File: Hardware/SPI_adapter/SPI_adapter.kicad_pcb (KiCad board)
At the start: 4 copper layers, 99.5 x 34.5 mm, 5 parts, among them J1 Conn_02x07_Top_Bottom, J2 Conn_Coaxial, U1 RF-LORA-868-SO

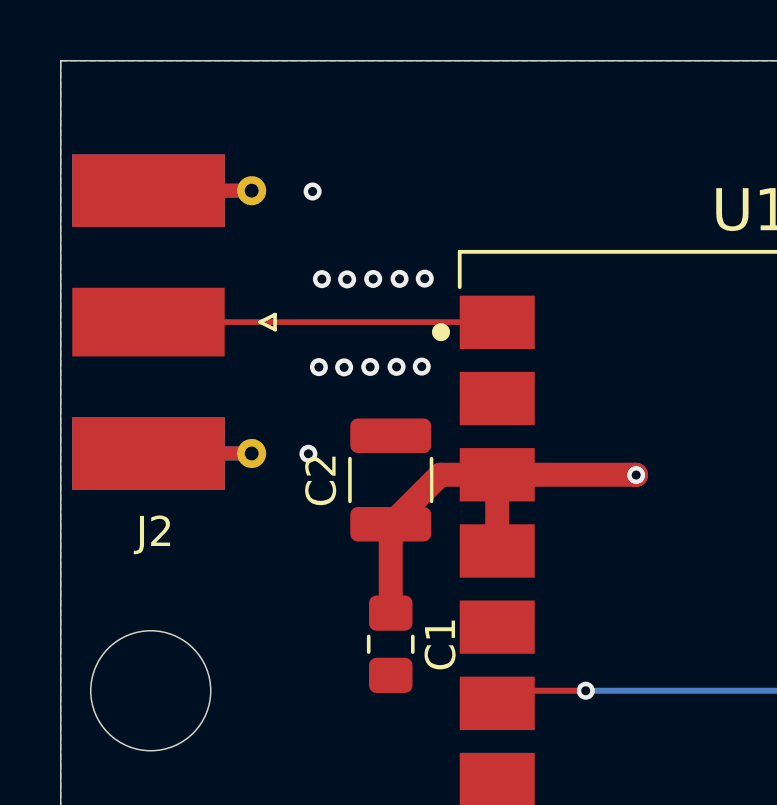
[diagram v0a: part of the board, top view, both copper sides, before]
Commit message: Fixed RF trace, Added new Diodes, better power traces and new switches
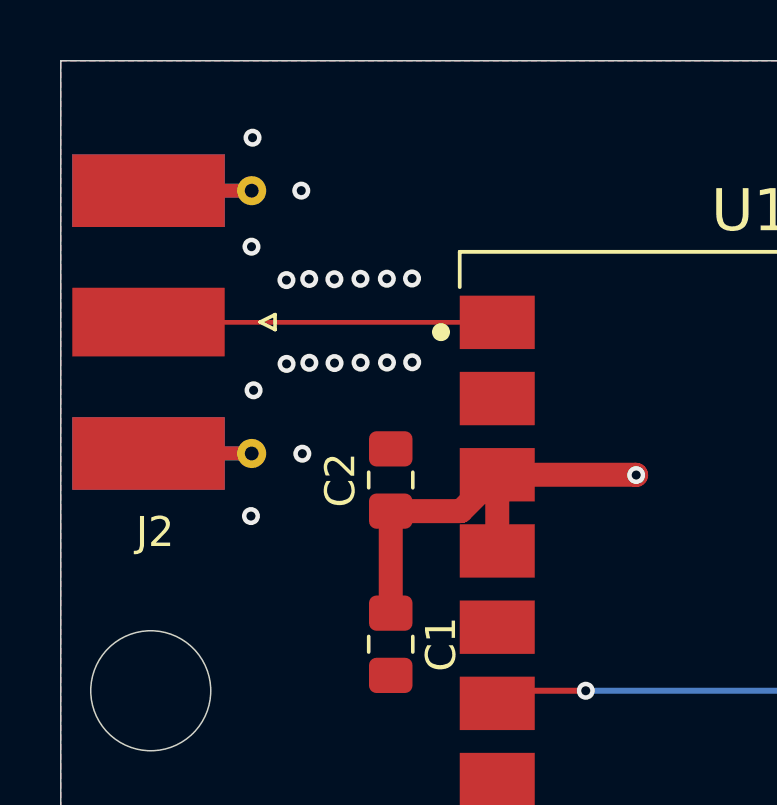
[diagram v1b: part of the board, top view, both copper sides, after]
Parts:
- C2: footprint Capacitor_SMD:C_1210_3225Metric -> Capacitor_SMD:C_0805_2012Metric_Pad1.18x1.45mm_HandSolder
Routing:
- net GND: vias 22 -> 28
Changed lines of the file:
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@@
 		)
 	)
-	(footprint "Capacitor_SMD:C_1210_3225Metric"
+	(footprint "Capacitor_SMD:C_0805_2012Metric_Pad1.18x1.45mm_HandSolder"
 		(layer "F.Cu")
 		(at 88.5 106.475 90)
-		(descr "Capacitor SMD 1210 (3225 Metric), square (rectangular) end terminal, IPC-7351 nominal, (Body size source: IPC-SM-782 page 76, https://www.pcb-3d.com/wordpress/wp-content/uploads/ipc-sm-782a_amendment_1_and_2.pdf), generated with kicad-footprint-generator")
-		(tags "capacitor")
+		(descr "Capacitor SMD 0805 (2012 Metric), square (rectangular) end terminal, IPC-7351 nominal with elongated pad for handsoldering. (Body size source: IPC-SM-782 page 76, https://www.pcb-3d.com/wordpress/wp-content/uploads/ipc-sm-782a_amendment_1_and_2.pdf, https://docs.google.com/spreadsheets/d/1BsfQQcO9C6DZCsRaXUlFlo91Tg2WpOkGARC1WS5S8t0/edit?usp=sharing), generated with kicad-footprint-generator")
+		(tags "capacitor handsolder")
 		(property "Reference" "C2"
-			(at 0 -2.3 90)
+			(at 0 -1.68 90)
 			(layer "F.SilkS")
 			(effects
@@
 		)
 		(property "Value" "4.7µF"
-			(at 0 2.3 90)
-			(layer "F.Fab")
-			(hide yes)
+			(at 0 1.68 90)
+			(layer "F.Fab")
 			(effects
 				(font
@@
 		(attr smd)
 		(fp_line
-			(start -0.711252 -1.36)
-			(end 0.711252 -1.36)
+			(start -0.261252 -0.735)
+			(end 0.261252 -0.735)
 			(stroke
 				(width 0.12)
@@
 		)
 		(fp_line
-			(start -0.711252 1.36)
-			(end 0.711252 1.36)
+			(start -0.261252 0.735)
+			(end 0.261252 0.735)
 			(stroke
 				(width 0.12)
@@
 		)
 		(fp_rect
-			(start -2.3 -1.6)
-			(end 2.3 1.6)
+			(start -1.88 -0.98)
+			(end 1.88 0.98)
 			(stroke
 				(width 0.05)
@@
 		)
 		(fp_rect
-			(start -1.6 -1.25)
-			(end 1.6 1.25)
+			(start -1 -0.625)
+			(end 1 0.625)
 			(stroke
 				(width 0.1)
@@
 			(effects
 				(font
-					(size 0.8 0.8)
-					(thickness 0.12)
+					(size 0.5 0.5)
+					(thickness 0.08)
 				)
 			)
 		)
 		(pad "1" smd roundrect
-			(at -1.475 0 90)
-			(size 1.15 2.7)
+			(at -1.0375 0 90)
+			(size 1.175 1.45)
 			(layers "F.Cu" "F.Mask" "F.Paste")
-			(roundrect_rratio 0.217391)
+			(roundrect_rratio 0.212766)
 			(net 1 "+3.3V")
 			(pintype "passive")
 		)
 		(pad "2" smd roundrect
-			(at 1.475 0 90)
-			(size 1.15 2.7)
+			(at 1.0375 0 90)
+			(size 1.175 1.45)
 			(layers "F.Cu" "F.Mask" "F.Paste")
-			(roundrect_rratio 0.217391)
+			(roundrect_rratio 0.212766)
 			(net 2 "GND")
 			(pintype "passive")
 		)
 		(embedded_fonts no)
-		(model "${KICAD9_3DMODEL_DIR}/Capacitor_SMD.3dshapes/C_1210_3225Metric.step"
+		(model "${KICAD9_3DMODEL_DIR}/Capacitor_SMD.3dshapes/C_0805_2012Metric.step"
 			(offset
 				(xyz 0 0 0)
@@
 	)
 	(segment
-		(start 92.05 106.3)
-		(end 90.15 106.3)
-		(width 0.8)
-		(layer "F.Cu")
-		(net 1)
-	)
-	(segment
 		(start 92.05 108.84)
 		(end 92.05 106.3)
@@
 	)
 	(segment
-		(start 90.15 106.3)
-		(end 88.5 107.95)
+		(start 90.8375 107.5125)
+		(end 92.05 106.3)
+		(width 0.8)
+		(layer "F.Cu")
+		(net 1)
+	)
+	(segment
+		(start 88.5 110.9125)
+		(end 88.5 107.5125)
 		(width 0.8)
 		(layer "F.Cu")
@@
 	)
 	(segment
-		(start 88.5 110.9125)
-		(end 88.5 107.95)
+		(start 88.5 107.5125)
+		(end 90.8375 107.5125)
 		(width 0.8)
 		(layer "F.Cu")
@@
 		(end 169.385 99)
 		(width 0.8)
-		(layer "In1.Cu")
+		(layer "In2.Cu")
 		(net 1)
 	)
@@
 		(end 103.99149 99)
 		(width 0.8)
-		(layer "In1.Cu")
+		(layer "In2.Cu")
 		(net 1)
 	)
@@
 		(end 172.5 102.115)
 		(width 0.8)
-		(layer "In1.Cu")
+		(layer "In2.Cu")
 		(net 1)
 	)
 	(via
-		(at 88.793948 99.771159)
+		(at 88.369767 99.766016)
 		(size 0.6)
 		(drill 0.3)
@@
 	)
 	(via
-		(at 88.694585 102.70361)
+		(at 88.374638 102.559484)
 		(size 0.6)
 		(drill 0.3)
@@
 	)
 	(via
-		(at 89.633619 99.762503)
-		(size 0.6)
-		(drill 0.3)
-		(layers "F.Cu" "B.Cu")
-		(free yes)
-		(net 2)
-	)
-	(via
-		(at 85.755918 105.601065)
-		(size 0.6)
-		(drill 0.3)
-		(layers "F.Cu" "B.Cu")
-		(free yes)
-		(net 2)
-	)
-	(via
-		(at 89.534256 102.694954)
-		(size 0.6)
-		(drill 0.3)
-		(layers "F.Cu" "B.Cu")
-		(free yes)
-		(net 2)
-	)
-	(via
-		(at 86.205681 99.779815)
+		(at 83.927854 103.484804)
+		(size 0.6)
+		(drill 0.3)
+		(layers "F.Cu" "B.Cu")
+		(free yes)
+		(net 2)
+	)
+	(via
+		(at 89.209438 99.75736)
+		(size 0.6)
+		(drill 0.3)
+		(layers "F.Cu" "B.Cu")
+		(free yes)
+		(net 2)
+	)
+	(via
+		(at 85.552404 105.598467)
+		(size 0.6)
+		(drill 0.3)
+		(layers "F.Cu" "B.Cu")
+		(free yes)
+		(net 2)
+	)
+	(via
+		(at 89.214309 102.550828)
+		(size 0.6)
+		(drill 0.3)
+		(layers "F.Cu" "B.Cu")
+		(free yes)
+		(net 2)
+	)
+	(via
+		(at 85.7815 99.774672)
 		(size 0.6)
 		(drill 0.3)
@@
 	)
 	(via
-		(at 87.8157 102.706495)
+		(at 87.495753 102.562369)
 		(size 0.6)
 		(drill 0.3)
@@
 	)
 	(via
+		(at 85.023414 99.81132)
+		(size 0.6)
+		(drill 0.3)
+		(layers "F.Cu" "B.Cu")
+		(free yes)
+		(net 2)
+	)
+	(via
 		(at 143.668627 102)
 		(size 0.6)
@@
 	)
 	(via
-		(at 87.915063 99.774044)
-		(size 0.6)
-		(drill 0.3)
-		(layers "F.Cu" "B.Cu")
-		(free yes)
-		(net 2)
-	)
-	(via
-		(at 87.045353 99.788472)
+		(at 87.490882 99.768901)
+		(size 0.6)
+		(drill 0.3)
+		(layers "F.Cu" "B.Cu")
+		(free yes)
+		(net 2)
+	)
+	(via
+		(at 86.621172 99.783329)
+		(size 0.6)
+		(drill 0.3)
+		(layers "F.Cu" "B.Cu")
+		(free yes)
+		(net 2)
+	)
+	(via
+		(at 83.892917 95.065089)
+		(size 0.6)
+		(drill 0.3)
+		(layers "F.Cu" "B.Cu")
+		(free yes)
+		(net 2)
+	)
+	(via
+		(at 83.840512 107.677193)
 		(size 0.6)
 		(drill 0.3)
@@
 	)
 	(via
-		(at 86.94599 102.720923)
+		(at 86.626043 102.576797)
 		(size 0.6)
 		(drill 0.3)
@@
 	)
 	(via
-		(at 86.106318 102.712266)
+		(at 85.028285 102.604788)
+		(size 0.6)
+		(drill 0.3)
+		(layers "F.Cu" "B.Cu")
+		(free yes)
+		(net 2)
+	)
+	(via
+		(at 85.786371 102.56814)
 		(size 0.6)
 		(drill 0.3)
@@
 	)
 	(via
-		(at 85.89442 96.858093)
+		(at 85.517468 96.829386)
+		(size 0.6)
+		(drill 0.3)
+		(layers "F.Cu" "B.Cu")
+		(free yes)
+		(net 2)
+	)
+	(via
+		(at 83.85798 98.698493)
 		(size 0.6)
 		(drill 0.3)
@@
 	)
 	(segment
-		(start 80.424493 101.211261)
-		(end 92.041261 101.211261)
+		(start 80.433232 101.22)
+		(end 80.424493 101.211261)
 		(width 0.19006)
+		(layer "F.Cu")
+		(net 15)
+	)
+	(segment
+		(start 92.05 101.22)
+		(end 80.433232 101.22)
+		(width 0.1565)
 		(layer "F.Cu")
 		(net 15)
@@
 	)
 	(zone
+		(net 0)
+		(net_name "")
+		(layer "F.Cu")
+		(hatch edge 0.5)
+		(connect_pads
+			(clearance 0)
+		)
+		(min_thickness 0.25)
+		(filled_areas_thickness no)
+		(keepout
+			(tracks allowed)
+			(vias allowed)
+			(pads allowed)
+			(copperpour not_allowed)
+			(footprints allowed)
+		)
+		(placement
+			(enabled no)
+			(sheetname "/")
+		)
+		(fill
+			(thermal_gap 0.5)
+			(thermal_bridge_width 0.5)
+		)
+		(polygon
+			(pts
+				(xy 83.074722 101.808385) (xy 83.07395 101.300185) (xy 90.288653 101.293981) (xy 90.289425 101.802181)
+			)
+		)
+	)
+	(zone
+		(net 0)
+		(net_name "")
+		(layer "F.Cu")
+		(hatch edge 0.5)
+		(connect_pads
+			(clearance 0)
+		)
+		(min_thickness 0.25)
+		(filled_areas_thickness no)
+		(keepout
+			(tracks allowed)
+			(vias allowed)
+			(pads allowed)
+			(copperpour not_allowed)
+			(footprints allowed)
+		)
+		(placement
+			(enabled no)
+			(sheetname "/")
+		)
+		(fill
+			(thermal_gap 0.5)
+			(thermal_bridge_width 0.5)
+		)
+		(polygon
+			(pts
+				(xy 83.081033 101.138651) (xy 83.080261 100.630451) (xy 90.294964 100.624247) (xy 90.295736 101.132447)
+			)
+		)
+	)
+	(zone

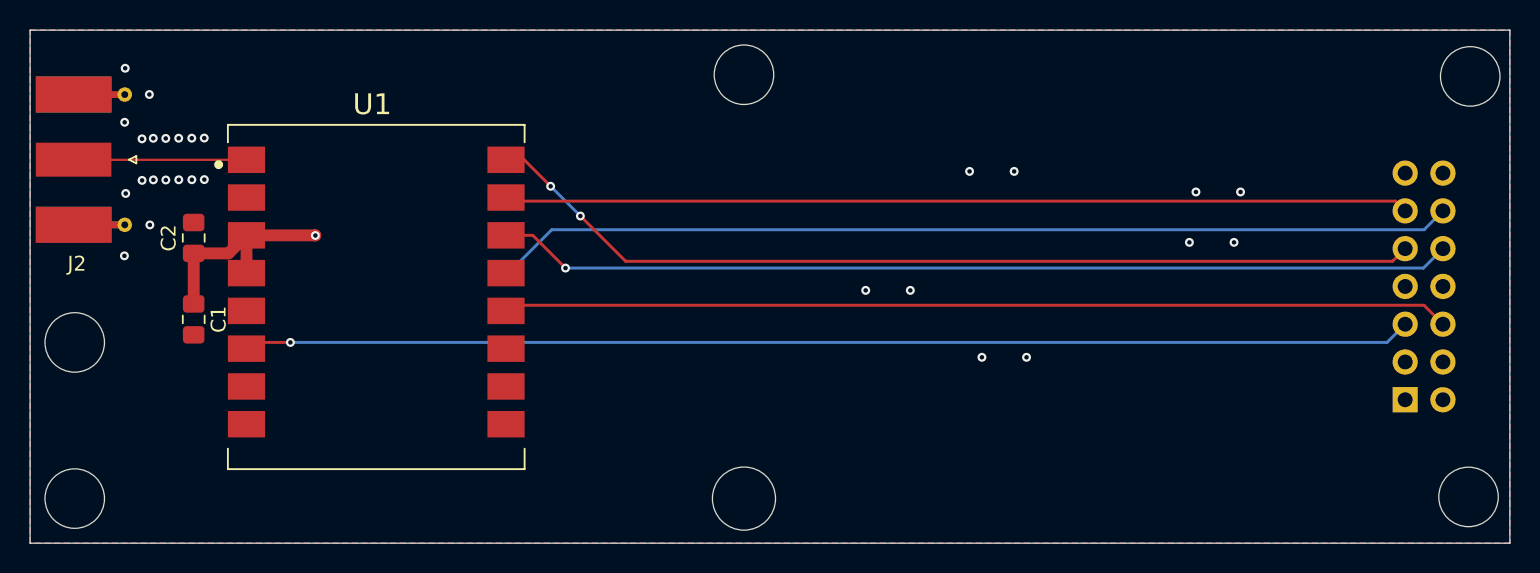
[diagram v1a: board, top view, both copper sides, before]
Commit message: Added HiPR logos and fixed mounting wholes
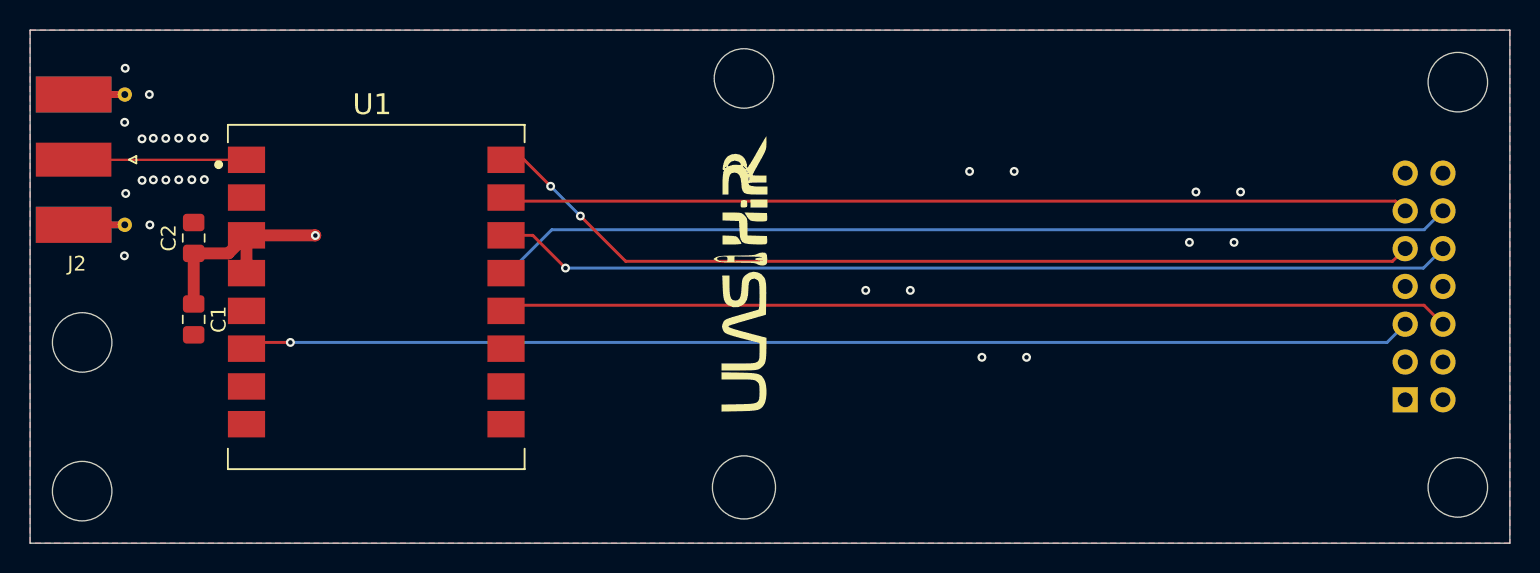
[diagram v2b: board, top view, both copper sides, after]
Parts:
- added G***: LOGO, MHF4_antenna:HiPR, F.Cu at (125.5, 109.0)
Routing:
- net +3.3V: track 94.8 -> 93.9 mm
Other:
- outline, holes or cut-outs redrawn

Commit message: SPI resistors removed and transmission added
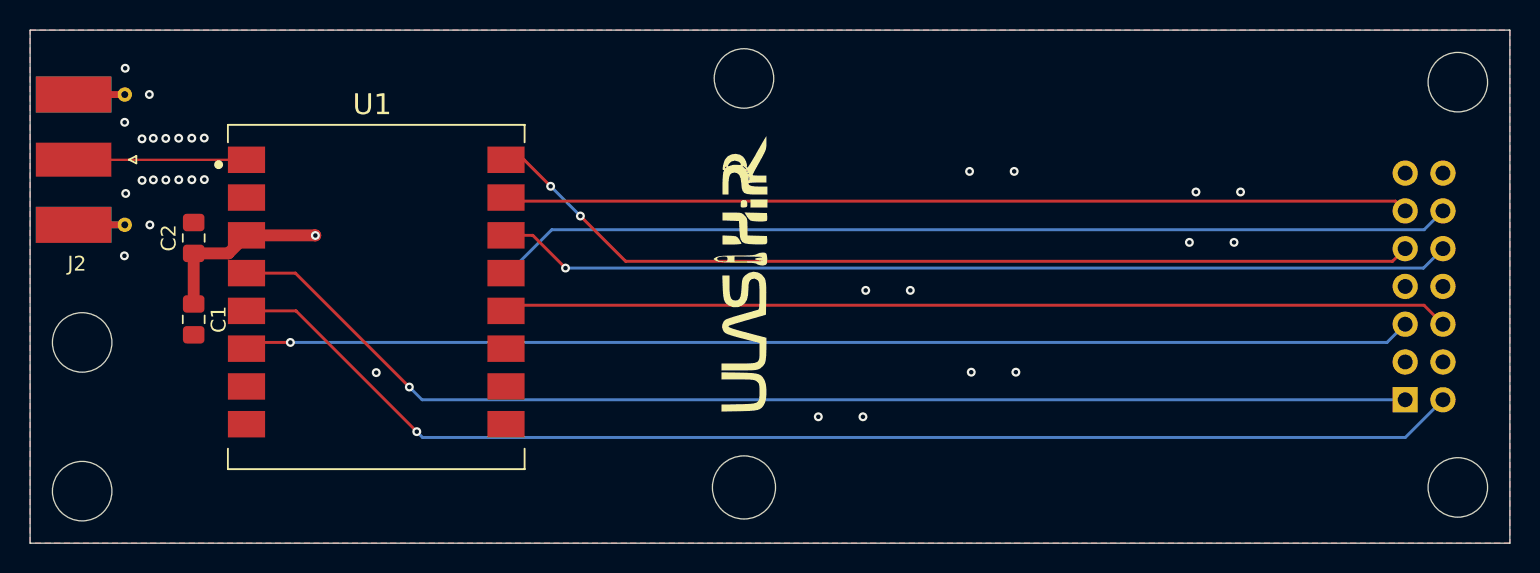
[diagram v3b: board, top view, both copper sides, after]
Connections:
- J1 pad 1: unconnected-(J1-Pin_1-Pad1) -> /RX_SWITCH
- J1 pad 2: unconnected-(J1-Pin_2-Pad2) -> /TX_SWITCH
- U1 pad 4: +3.3V -> /RX_SWITCH
- U1 pad 5: GND -> /TX_SWITCH
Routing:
- net /TX_SWITCH: track 0.00 -> 85.0 mm, vias 0 -> 1
- net /RX_SWITCH: track 0.00 -> 81.4 mm, vias 0 -> 1
- net +3.3V: track 93.9 -> 91.4 mm
- net GND: vias 28 -> 31
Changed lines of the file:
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@@
 	(net 3 "/RADIO_RST")
 	(net 4 "/SPI_SCK")
-	(net 5 "unconnected-(J1-Pin_1-Pad1)")
+	(net 5 "/RX_SWITCH")
 	(net 6 "/RADIO_TX")
-	(net 7 "unconnected-(J1-Pin_2-Pad2)")
+	(net 7 "/TX_SWITCH")
 	(net 8 "/SPI_MISO")
 	(net 9 "/SPI_MOSI")
@@
 			(size 2.5 1.78)
 			(layers "F.Cu" "F.Mask" "F.Paste")
-			(net 1 "+3.3V")
+			(net 5 "/RX_SWITCH")
 			(pinfunction "RX_SWITCH")
 			(pintype "input")
@@
 			(size 2.5 1.78)
 			(layers "F.Cu" "F.Mask" "F.Paste")
-			(net 2 "GND")
+			(net 7 "/TX_SWITCH")
 			(pinfunction "TX_SWITCH")
 			(pintype "input")
@@
 			(layers "*.Cu" "*.Mask")
 			(remove_unused_layers no)
-			(net 5 "unconnected-(J1-Pin_1-Pad1)")
+			(net 5 "/RX_SWITCH")
 			(pinfunction "Pin_1")
-			(pintype "passive+no_connect")
+			(pintype "passive")
 		)
 		(pad "2" thru_hole circle
@@
 			(layers "*.Cu" "*.Mask")
 			(remove_unused_layers no)
-			(net 7 "unconnected-(J1-Pin_2-Pad2)")
+			(net 7 "/TX_SWITCH")
 			(pinfunction "Pin_2")
-			(pintype "passive+no_connect")
+			(pintype "passive")
 		)
 		(pad "3" thru_hole circle
@@
 	)
 	(segment
-		(start 92.05 108.84)
-		(end 92.05 106.3)
-		(width 0.8)
-		(layer "F.Cu")
-		(net 1)
-	)
-	(segment
 		(start 90.8375 107.5125)
 		(end 92.05 106.3)
@@
 	)
 	(via
-		(at 144.5 114.5)
+		(at 143.782939 115.500414)
 		(size 0.6)
 		(drill 0.3)
@@
 	)
 	(via
+		(at 133.5 118.5)
+		(size 0.6)
+		(drill 0.3)
+		(layers "F.Cu" "B.Cu")
+		(free yes)
+		(net 2)
+	)
+	(via
 		(at 83.840512 107.677193)
 		(size 0.6)
@@
 	)
 	(via
+		(at 100.773836 115.529493)
+		(size 0.6)
+		(drill 0.3)
+		(layers "F.Cu" "B.Cu")
+		(free yes)
+		(net 2)
+	)
+	(via
 		(at 86.626043 102.576797)
 		(size 0.6)
@@
 	)
 	(via
-		(at 141.5 114.5)
+		(at 140.782939 115.500414)
 		(size 0.6)
 		(drill 0.3)
@@
 	(via
 		(at 83.85798 98.698493)
+		(size 0.6)
+		(drill 0.3)
+		(layers "F.Cu" "B.Cu")
+		(free yes)
+		(net 2)
+	)
+	(via
+		(at 130.5 118.5)
 		(size 0.6)
 		(drill 0.3)
@@
 	)
 	(segment
+		(start 95.34 108.84)
+		(end 103 116.5)
+		(width 0.2)
+		(layer "F.Cu")
+		(net 5)
+	)
+	(segment
+		(start 92.05 108.84)
+		(end 95.34 108.84)
+		(width 0.2)
+		(layer "F.Cu")
+		(net 5)
+	)
+	(via
+		(at 103 116.5)
+		(size 0.6)
+		(drill 0.3)
+		(layers "F.Cu" "B.Cu")
+		(net 5)
+	)
+	(segment
+		(start 103 116.5)
+		(end 103.855 117.355)
+		(width 0.2)
+		(layer "B.Cu")
+		(net 5)
+	)
+	(segment
+		(start 103.855 117.355)
+		(end 169.96 117.355)
+		(width 0.2)
+		(layer "B.Cu")
+		(net 5)
+	)
+	(segment
+		(start 95.38 111.38)
+		(end 103.5 119.5)
+		(width 0.2)
+		(layer "F.Cu")
+		(net 7)
+	)
+	(segment
+		(start 92.05 111.38)
+		(end 95.38 111.38)
+		(width 0.2)
+		(layer "F.Cu")
+		(net 7)
+	)
+	(via
+		(at 103.5 119.5)
+		(size 0.6)
+		(drill 0.3)
+		(layers "F.Cu" "B.Cu")
+		(net 7)
+	)
+	(segment
+		(start 103.890763 119.890763)
+		(end 169.964237 119.890763)
+		(width 0.2)
+		(layer "B.Cu")
+		(net 7)
+	)
+	(segment
+		(start 169.964237 119.890763)
+		(end 172.5 117.355)
+		(width 0.2)
+		(layer "B.Cu")
+		(net 7)
+	)
+	(segment
+		(start 103.5 119.5)
+		(end 103.890763 119.890763)
+		(width 0.2)
+		(layer "B.Cu")
+		(net 7)
+	)
+	(segment

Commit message: hardware done
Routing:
- added copper zone on In2.Cu, net GND
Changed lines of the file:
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@@
 			(drillshape 0)
 			(scaleselection 1)
-			(outputdirectory "../Manufacturing/SPI_adapter/Gerber Output/")
+			(outputdirectory "../Manufacturing/SPI_adapter/fabrication/")
 		)
 	)
@@
 		(net 2)
 		(net_name "GND")
-		(layer "F.Cu")
+		(layers "F.Cu" "B.Cu" "In1.Cu" "In2.Cu")
 		(hatch edge 0.5)
 		(priority 2)
